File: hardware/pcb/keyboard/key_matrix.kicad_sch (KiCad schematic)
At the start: 75 parts, among them SW1 EC_SW, SW10 EC_SW, SW11 EC_SW, SW12 EC_SW, SW13 EC_SW, SW14 EC_SW, SW15 EC_SW, SW16 EC_SW, SW17 EC_SW, SW18 EC_SW, SW19 EC_SW, SW2 EC_SW, SW20 EC_SW, SW21 EC_SW, SW22 EC_SW, SW23 EC_SW, SW24 EC_SW, SW25 EC_SW, SW26 EC_SW, SW27 EC_SW, SW3 EC_SW, SW4 EC_SW, SW5 EC_SW, SW6 EC_SW, SW7 EC_SW, SW8 EC_SW, SW9 EC_SW

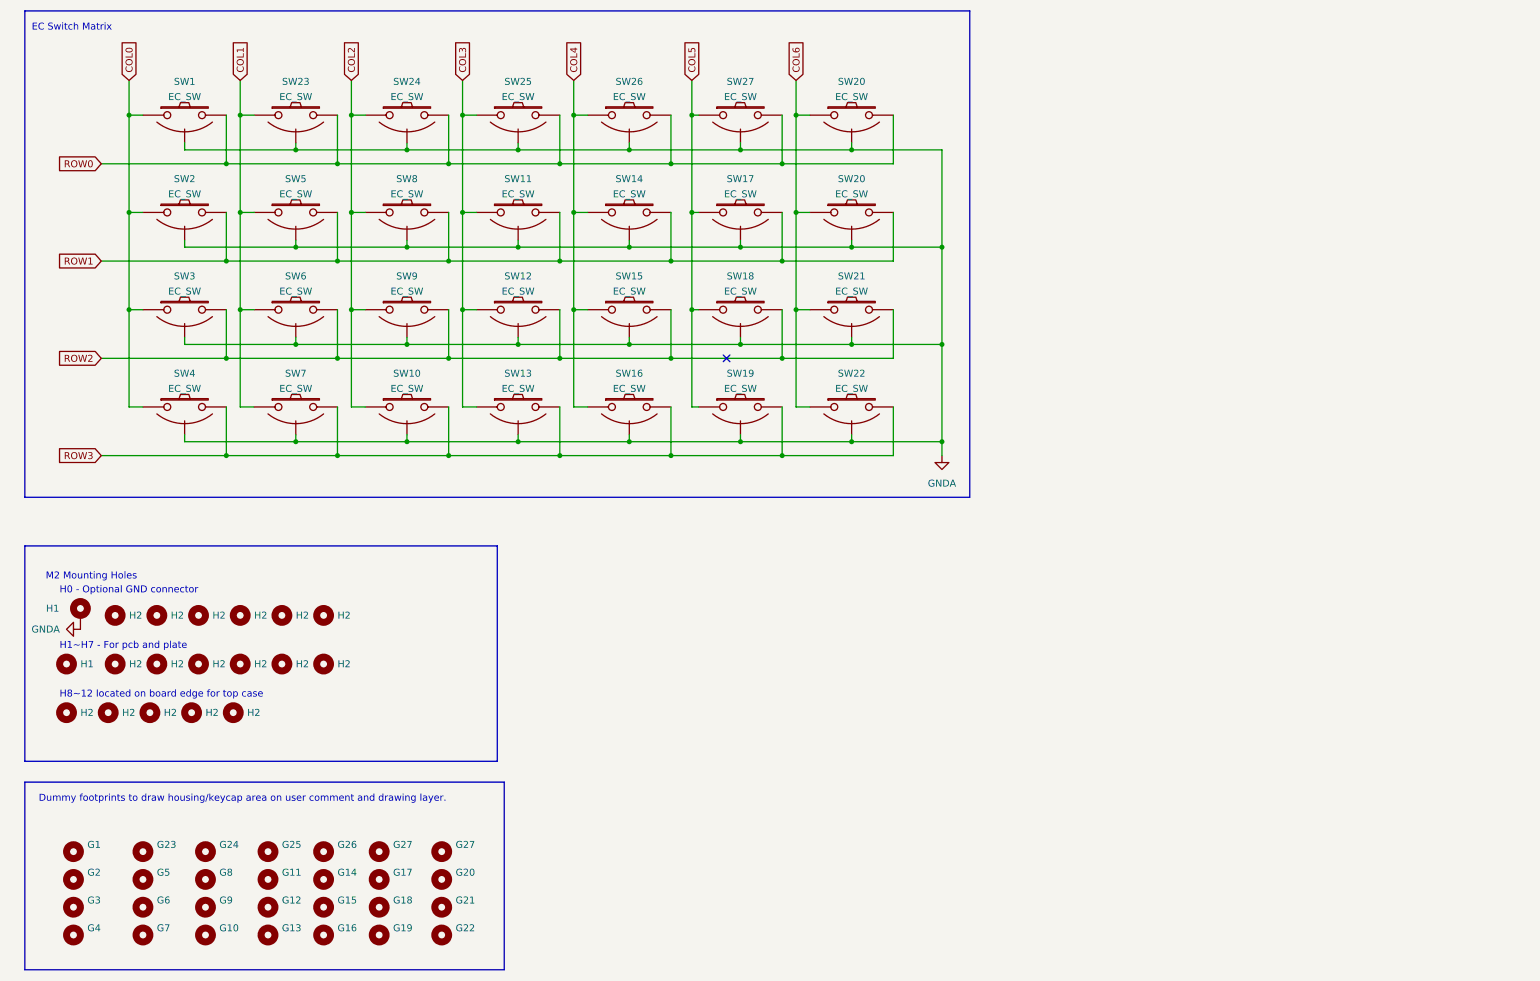
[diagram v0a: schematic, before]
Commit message: Init STM32G0 PCB
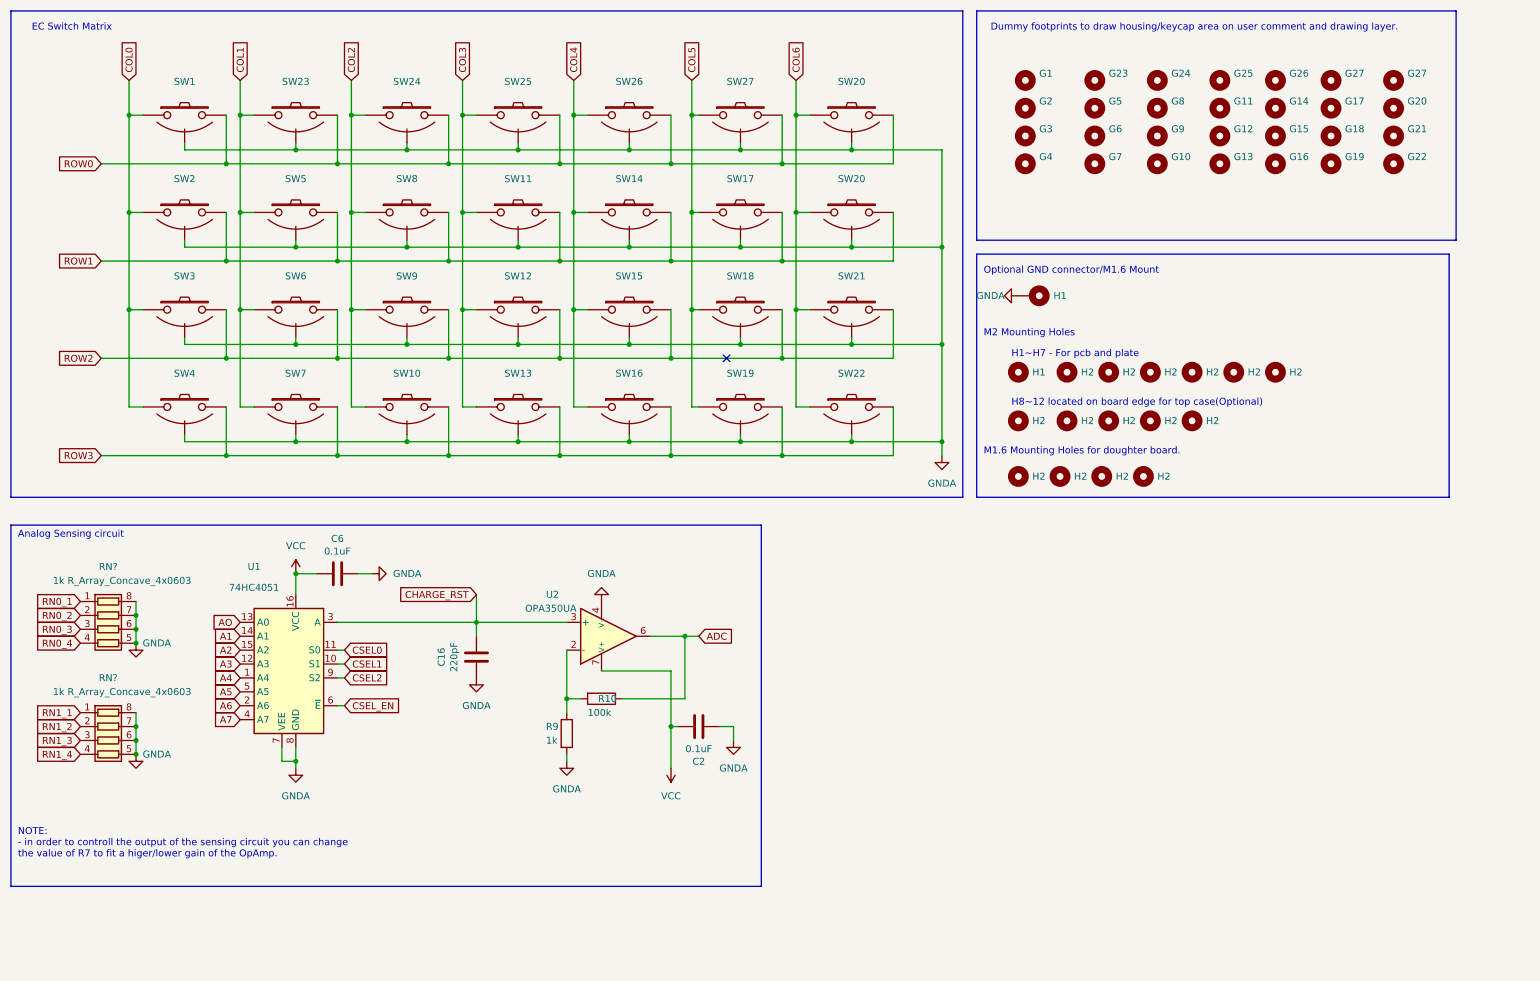
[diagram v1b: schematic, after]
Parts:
- removed H2 (x2): ~, ec_parts:SMT-SO-M1.6-screwhole_only, symbol Mechanical:MountingHole
- added C16: 220pF, PCM_Capacitor_SMD_AKL:C_0603_1608Metric_Pad1.05x0.95mm, symbol Device:C
- added C2, C6: 0.1uF, PCM_Capacitor_SMD_AKL:C_0603_1608Metric_Pad1.05x0.95mm, symbol Device:C
- added R10: 100k, PCM_Resistor_SMD_AKL:R_0603_1608Metric_Pad0.98x0.95mm, symbol Device:R
- added R9: 1k, PCM_Resistor_SMD_AKL:R_0603_1608Metric_Pad0.98x0.95mm, symbol Device:R
- added RN? (x2): 1k R_Array_Concave_4x0603, PCM_Resistor_SMD_AKL:R_Array_Concave_4x0603, symbol PCM_Resistor_AKL:R_4x0612_Convex
- added U1: 74HC4051, PCM_Package_SO_AKL:TSSOP-16_4.4x5mm_P0.65mm, symbol 74xx:74HC4051
- added U2: OPA350UA, PCM_Package_SO_AKL:SO-8_3.9x4.9mm_P1.27mm, symbol PCM_Amplifier_Operational_AKL:OPA350UA
- H1, H2: footprint MountingHole:MountingHole_2.1mm -> ec_parts:MountingHole_2.05mm
- SW1, SW10, SW11, SW12, SW13, SW14, SW15, SW16, SW17, SW18, SW19, SW2, SW20, SW21, SW22, SW23, SW24, SW25, SW26, SW27, SW3, SW4, SW5, SW6, SW7, SW8, SW9: value EC_SW -> ~
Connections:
- net GNDA: now also C16.2, C2.1, C6.1, R9.2, RN?.5 (R4.2), RN?.5 (R4.2), RN?.6 (R3.2), RN?.6 (R3.2), RN?.7 (R2.2), RN?.7 (R2.2), RN?.8 (R1.2), RN?.8 (R1.2), U1.7 (VEE), U1.8 (GND), U2.4 (V-)
- new net: R10.2, R9.1, U2.2 (-)
- new net A1: U1.14 (A1)
- new net A2: U1.15 (A2)
- new net A3: U1.12 (A3)
- new net A4: U1.1 (A4)
- new net A5: U1.5 (A5)
- new net A6: U1.2 (A6)
- new net A7: U1.4 (A7)
- new net ADC: R10.1, U2.6
- new net AO: U1.13 (A0)
- new net CHARGE_RST: C16.1, U1.3 (A), U2.3 (+)
- new net CSEL0: U1.11 (S0)
- new net CSEL1: U1.10 (S1)
- new net CSEL2: U1.9 (S2)
- new net CSEL_EN: U1.6 (~{E})
- new net RN0_1: RN?.1 (R1.1)
- new net RN0_2: RN?.2 (R2.1)
- new net RN0_3: RN?.3 (R3.1)
- new net RN0_4: RN?.4 (R4.1)
- new net RN1_1: RN?.1 (R1.1)
- new net RN1_2: RN?.2 (R2.1)
- new net RN1_3: RN?.3 (R3.1)
- new net RN1_4: RN?.4 (R4.1)
- new net VCC: C2.2, C6.2, U1.16 (VCC), U2.7 (V+)
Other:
- note added: "Analog Sensing circuit"
- note added: "H8~12 located on board edge for top case(Optional)"
- note added: "M1.6 Mounting Holes for doughter board."
- note added: "NOTE: - in order to controll the output of the sensing circuit you can change the value of R7 to fit a higer/lower gain of the OpAmp."
- note added: "Optional GND connector/M1.6 Mount"
- note removed: "H0 - Optional GND connector"
- note removed: "H8~12 located on board edge for top case"
- moved on the sheet: G1, G10, G11, G12, G13, G14, G15, G16, G17, G18, G19, G2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

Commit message: Fix capacitor, resistor values
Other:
- title: (none) -> Key Matrix
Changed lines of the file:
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@@
   (paper "A4")
   (title_block
-    (date "2022-12-24")
+    (title "Key Matrix")
+    (date "2023-07-18")
     (rev "1.0")
     (comment 2 "MIT License")

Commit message: init
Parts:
- removed H2 (x3): ~, ec_parts:SMT-SO-M1.6-screwhole_only, symbol Mechanical:MountingHole
- added H14, H15, H16: ~, ec_parts:MountingHole_2.05mm, symbol Mechanical:MountingHole
- H13: renamed from H2; footprint ec_parts:SMT-SO-M1.6-screwhole_only -> ec_parts:MountingHole_2.05mm
- gave numbers to parts that had none: 2
- renumbered C16 to C10, C6 to C2, C2 to C3, G27 to G28, H1 to H0, H2 to H10, H2 to H11, H2 to H12, H2 to H3, H2 to H4, H2 to H5, H2 to H6, H2 to H7, H2 to H8, H2 to H9, R9 to R6, R10 to R7, SW20 to SW28
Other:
- note added: "Mounting Holes for doughter board."
- note removed: "M1.6 Mounting Holes for doughter board."
